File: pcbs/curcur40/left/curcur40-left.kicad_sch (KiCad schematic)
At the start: 79 parts, among them J1 TYPE-C-31-M-13C, J2 TRS, J4 Conn_01x03, SW1 SW_Push, SW10 SW_Push, SW11 SW_Push, SW12 SW_Push, SW13 SW_Push, SW14 SW_Push, SW15 SW_Push, SW16 SW_Push, SW17 SW_Push, SW18 SW_Push, SW2 SW_Push, SW3 SW_Push, SW4 SW_Push, SW5 SW_Push, SW6 SW_Push, SW7 SW_Push, SW8 SW_Push, SW9 SW_Push, U1 RP2040, U2 NCP1117LPST33T3G, U3 TPD4E05U06DQAR, U4 W25Q128JVSIQ, Y1 12MHz 18pF

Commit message: fix
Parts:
- U4: footprint Package_SO:SOIC-8_5.23x5.23mm_P1.27mm -> Package_SO:SOIC-8_5.3x5.3mm_P1.27mm
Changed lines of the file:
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@@
 			)
 		)
-		(property "Footprint" "Package_SO:SOIC-8_5.23x5.23mm_P1.27mm"
+		(property "Footprint" "Package_SO:SOIC-8_5.3x5.3mm_P1.27mm"
 			(at 233.68 55.88 0)
 			(hide yes)

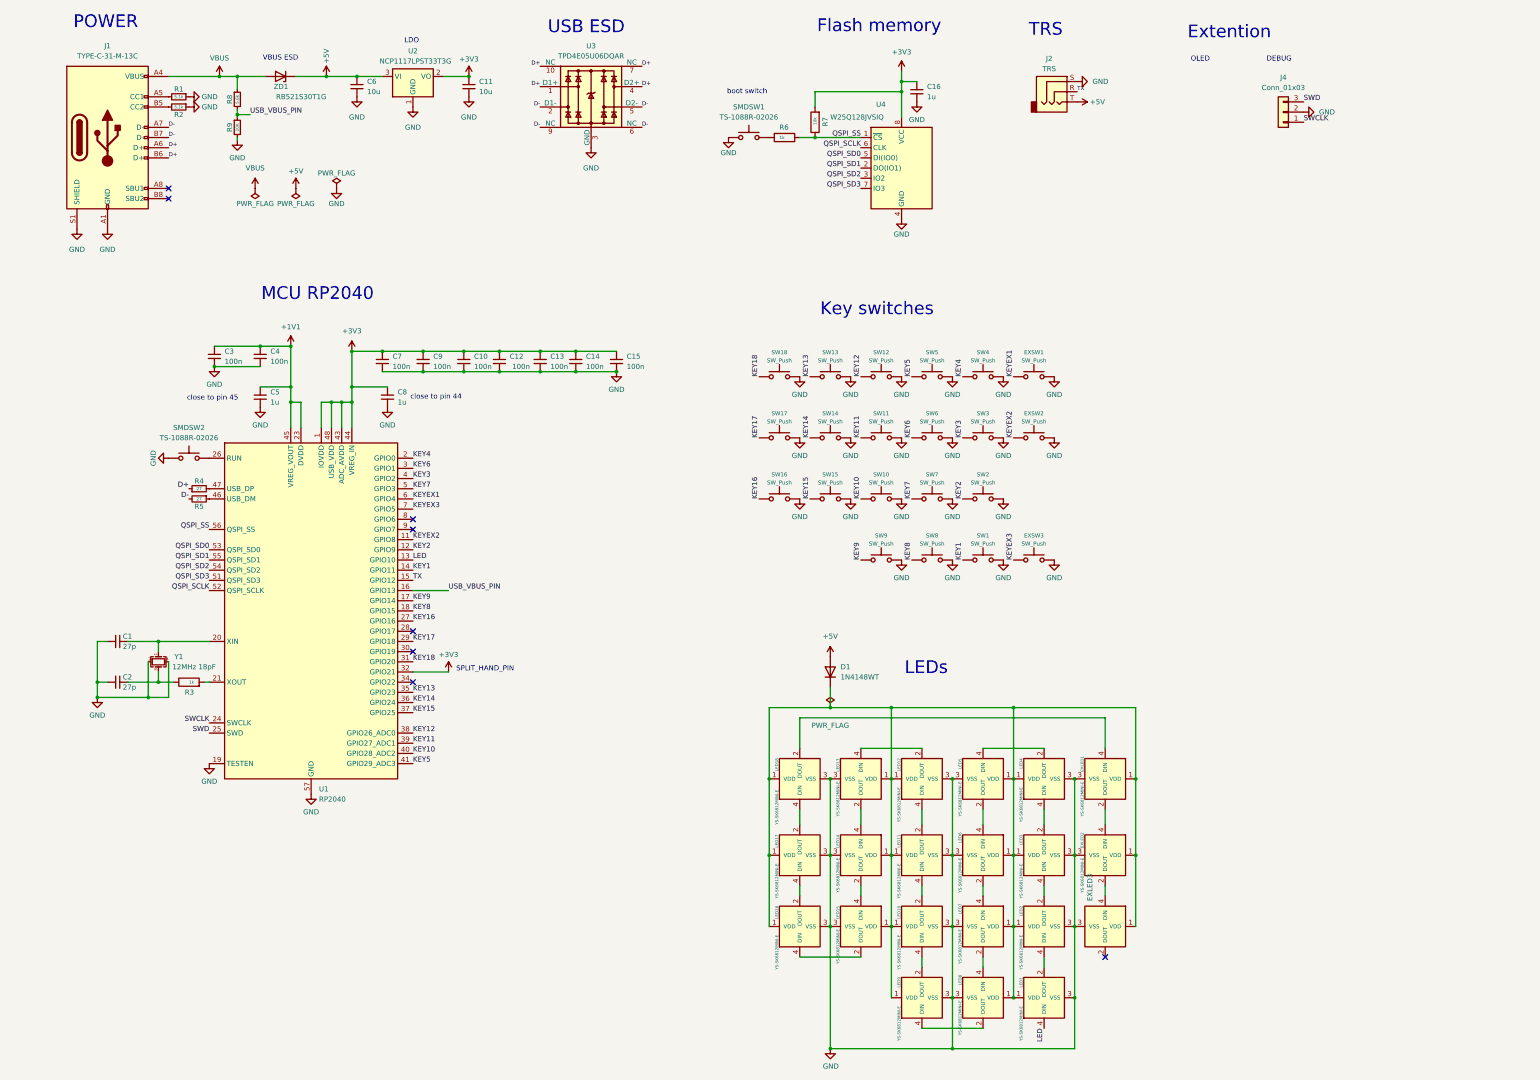
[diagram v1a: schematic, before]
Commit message: fix(pcb): eliminate all ERC/DRC/parity warnings and ignored DRC checks on left and right PCBs
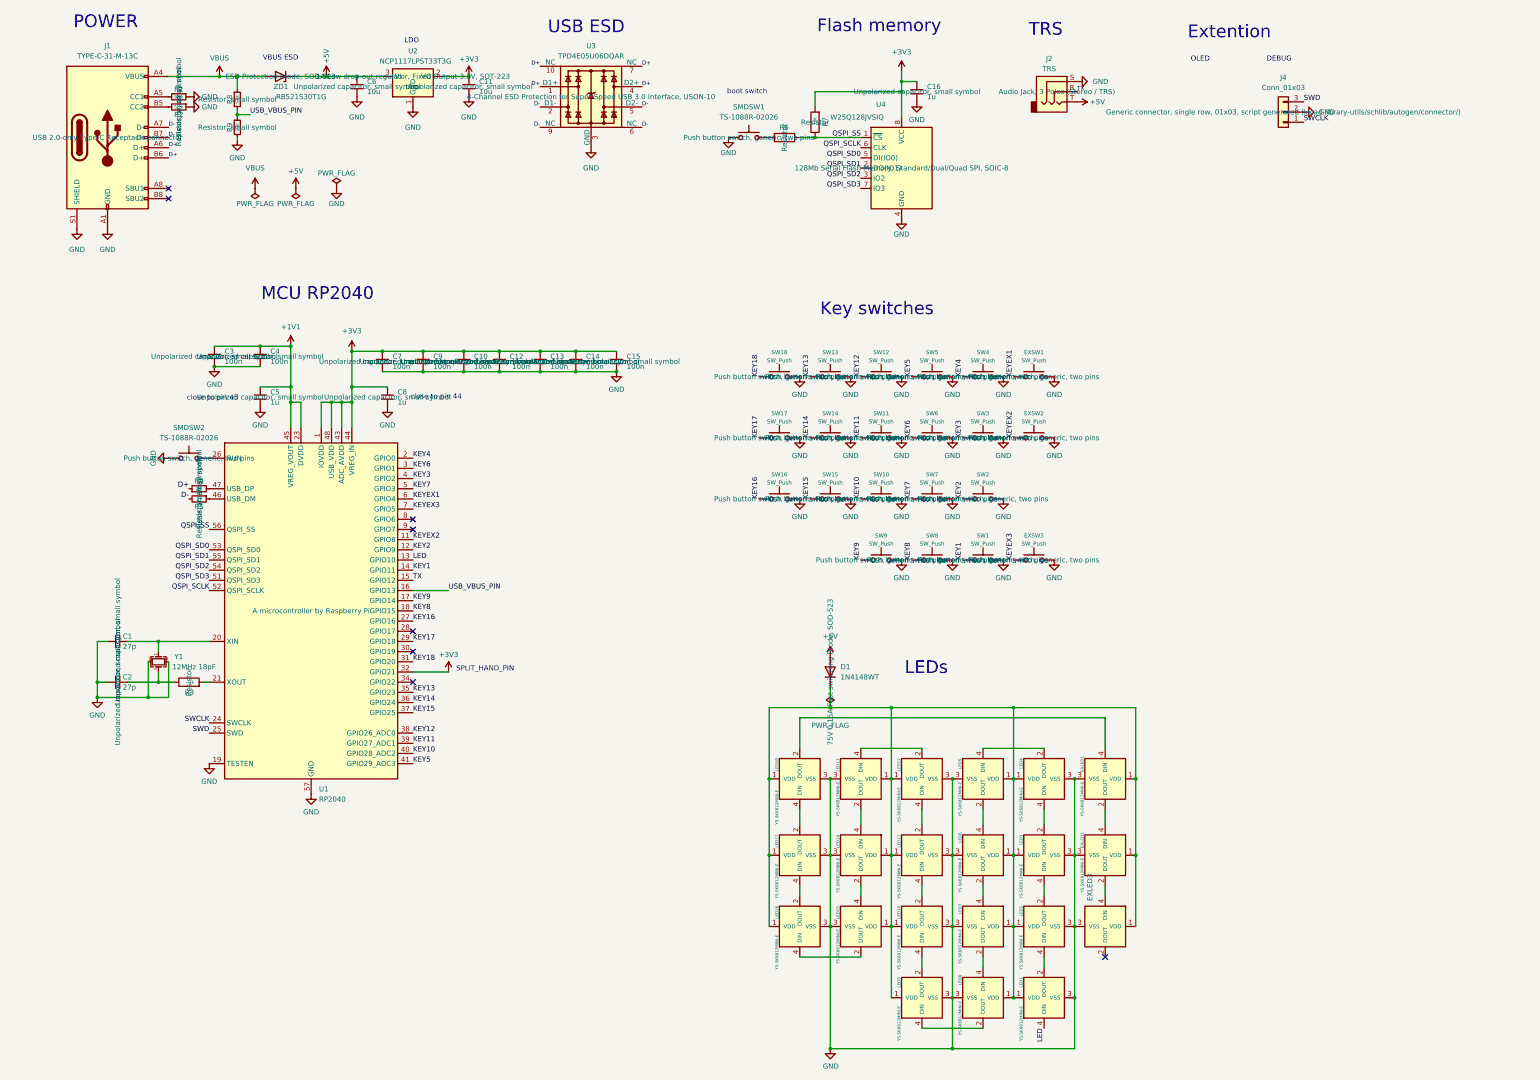
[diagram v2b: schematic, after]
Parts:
- LED9: footprint kbd_local:YS-SK6812MINI-E -> kbd_local:YS-SK6812MINI-E_LED9
- SW1: footprint kbd_local:keyswitch_choc12_hotswap_1u -> kbd_local:keyswitch_choc12_hotswap_1.5u
- Y1: footprint Crystal:Crystal_SMD_3225-4Pin_3.2x2.5mm -> Crystal:Crystal_SMD_3225-4Pin_3.2x2.5mm_Left

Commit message: Refactor PCBs and schematics to use genuine KiCad 10.0 standard libraries and isolate PMW3360 VDDPIX
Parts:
- EXLED1, EXLED2, EXLED3, LED1, LED10, LED11, LED12, LED13, LED14, LED15, LED16, LED17, LED18, LED2, LED3, LED4, LED5, LED6, LED7, LED8: footprint kbd_local:YS-SK6812MINI-E -> kbd:YS-SK6812MINI-E; symbol kbd_local:YS-SK6812MINI-E -> kbd:YS-SK6812MINI-E
- EXSW1, EXSW2, EXSW3, SW10, SW11, SW12, SW13, SW14, SW15, SW16, SW17, SW18, SW2, SW3, SW4, SW5, SW6, SW7, SW8, SW9: footprint kbd_local:keyswitch_choc12_hotswap_1u -> kbd:keyswitch_choc12_hotswap_1u
- J1: footprint kbd_local:TYPE-C-31-M-13C -> kbd:USB_C_Receptacle_TYPE-C-31-M-13C; symbol Connector:USB_C_Receptacle_USB2.0 -> Connector:USB_C_Receptacle_USB2.0_16P
- J2: footprint kbd_local:PJ-398A-5A_PJ-399B-6A -> kbd:Jack_PJ-398A-5A_PJ-399B-6A
- LED9: footprint kbd_local:YS-SK6812MINI-E_LED9 -> kbd:YS-SK6812MINI-E_LED9; symbol kbd_local:YS-SK6812MINI-E -> kbd:YS-SK6812MINI-E
- SMDSW1, SMDSW2: footprint kbd_local:TS-1088R-02026 -> kbd:TS-1088R-02026
- SW1: footprint kbd_local:keyswitch_choc12_hotswap_1.5u -> kbd:keyswitch_choc12_hotswap_1.5u
- Y1: footprint Crystal:Crystal_SMD_3225-4Pin_3.2x2.5mm_Left -> Crystal:Crystal_SMD_3225-4Pin_3.2x2.5mm
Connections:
- net GND: now also J1.SH (SHIELD); no longer J1.S1 (SHIELD)
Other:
- moved on the sheet: C1, C2, R3, R4, R5, SMDSW2, U4

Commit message: Clean up unused custom library files, fix fp-lib-table, and mark SWD headers J4/rJ4 as DNP
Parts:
- J4: now not fitted; now left out of the parts list
- LED9: footprint kbd:YS-SK6812MINI-E_LED9 -> kbd:YS-SK6812MINI-E
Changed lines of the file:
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@@
 			)
 		)
-		(property "Footprint" "kbd:YS-SK6812MINI-E_LED9"
+		(property "Footprint" "kbd:YS-SK6812MINI-E"
 			(at 245.11 260.35 0)
 			(hide yes)
@@
 		(body_style 1)
 		(exclude_from_sim no)
-		(in_bom yes)
-		(on_board yes)
-		(in_pos_files yes)
-		(dnp no)
+		(in_bom no)
+		(on_board yes)
+		(in_pos_files yes)
+		(dnp yes)
 		(fields_autoplaced yes)
 		(property "Reference" "J4"

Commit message: Unify SW1/rSW1 to 1u Choc footprint and document curcur40 component specs and sourcing in pcb_spec.md
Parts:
- SW1: footprint kbd:keyswitch_choc12_hotswap_1.5u -> kbd:keyswitch_choc12_hotswap_1u
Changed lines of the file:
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@@
 			)
 		)
-		(property "Footprint" "kbd:keyswitch_choc12_hotswap_1.5u"
+		(property "Footprint" "kbd:keyswitch_choc12_hotswap_1u"
 			(at 254 148.59 0)
 			(hide yes)

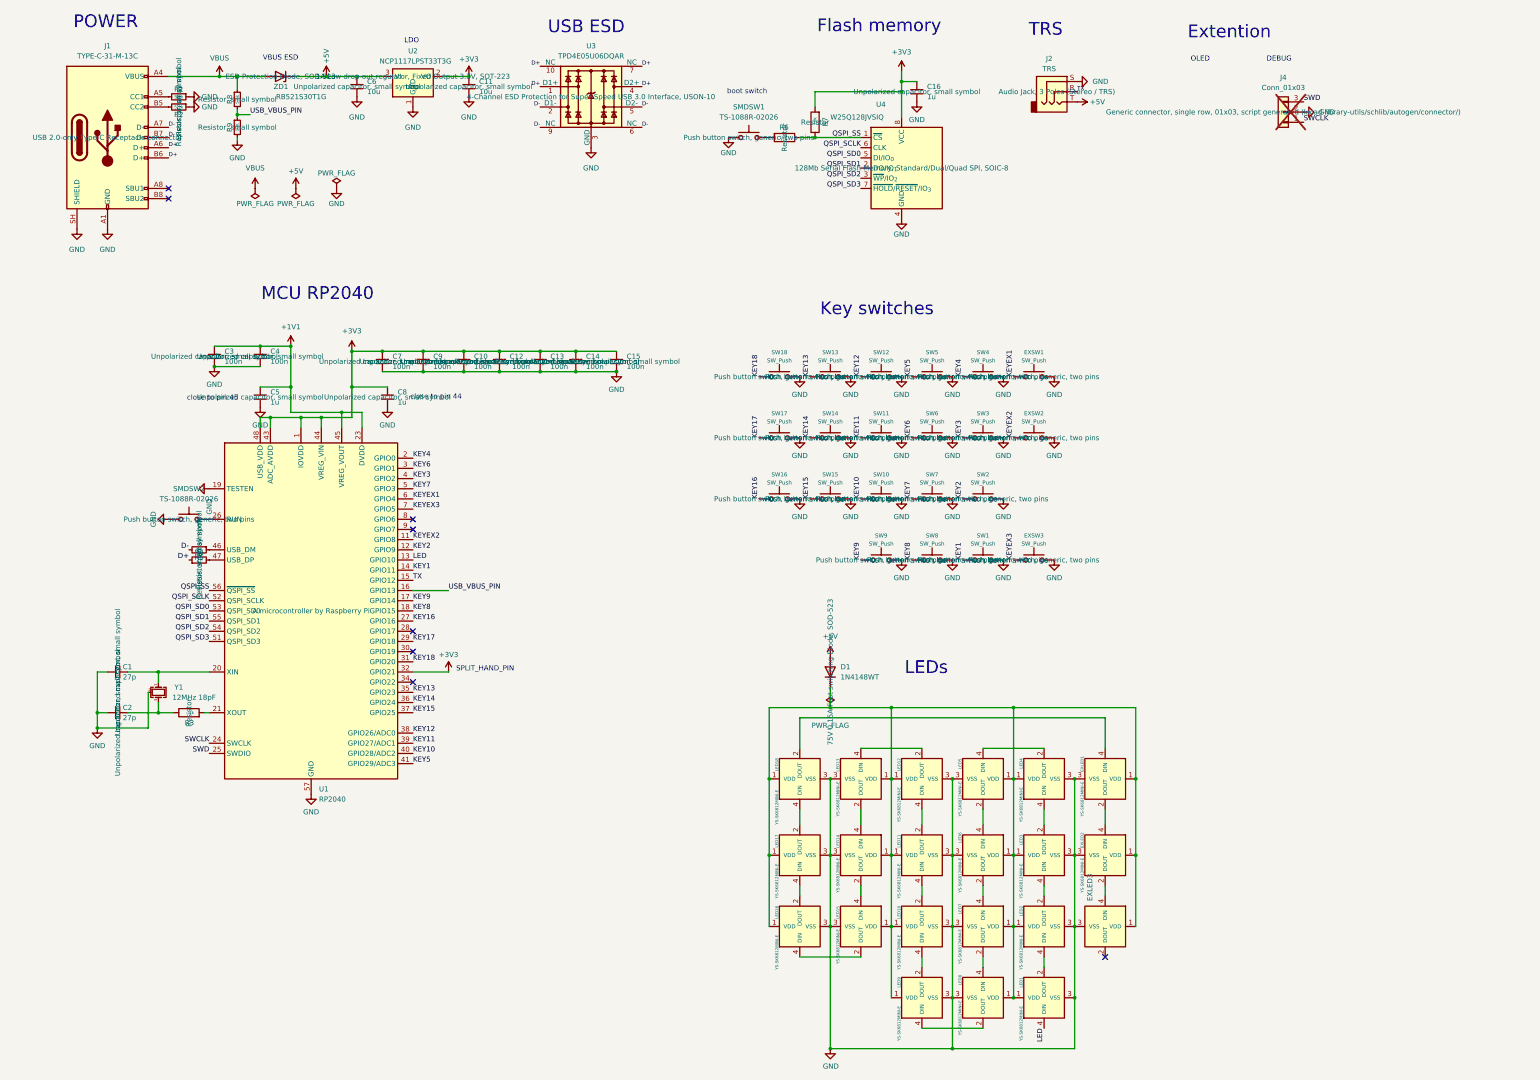
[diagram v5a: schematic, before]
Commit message: fix(pcb): resolve all ERC off-grid/four-way-junction warnings and restore PCB symbol UUID paths
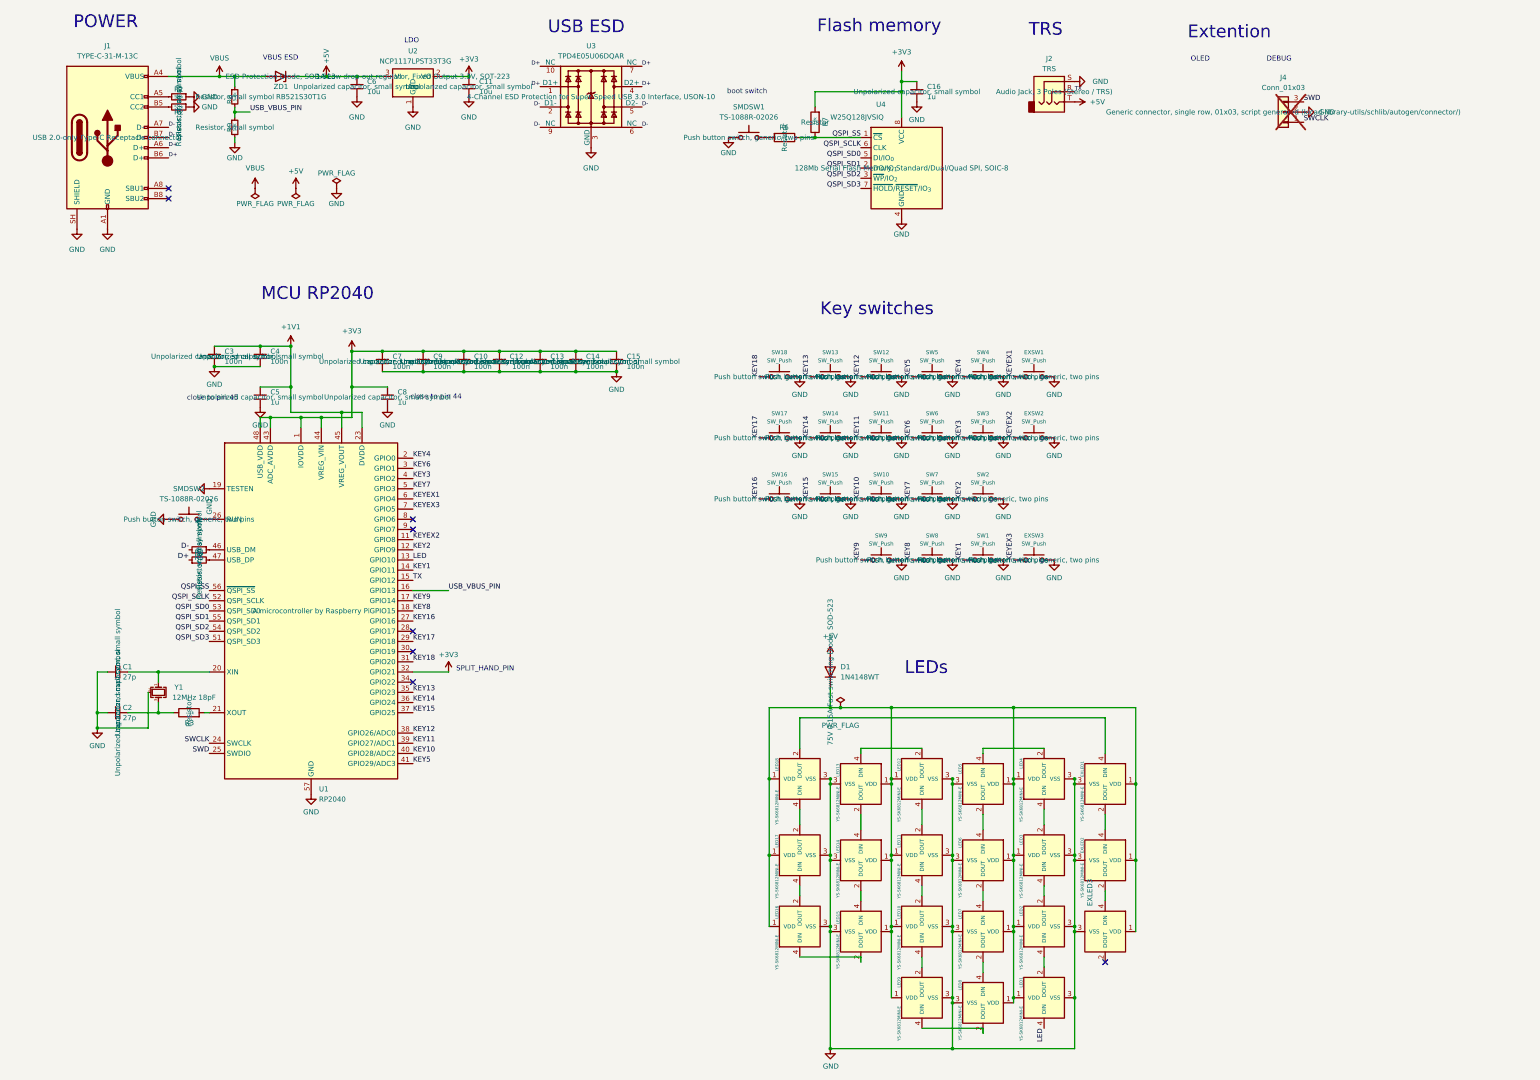
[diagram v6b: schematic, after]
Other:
- moved on the sheet: EXLED1, EXLED2, EXLED3, J2, LED13, LED14, LED15, LED5, LED6, LED7, LED8, R8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
